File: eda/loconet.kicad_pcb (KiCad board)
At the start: 4 copper layers, 105.7 x 60.2 mm, 69 parts, among them J1 RJ12, J10 FROG4, J11 LN Debug, J12 LN Raw, J13 Input voltage, J2 DCC IN, J3 FROG1, J4 DCC1, J5 FROG2, J6 DCC2, J7 DCC3, J8 FROG3, J9 DCC4, Q2 MMBT3904, U1 LM311, U2 MOUDLE-SEEEDUINO-XIAO, U3 L78M05ABDT-TR, U4 6N139, U5 6N139, U6 6N139, U7 6N139

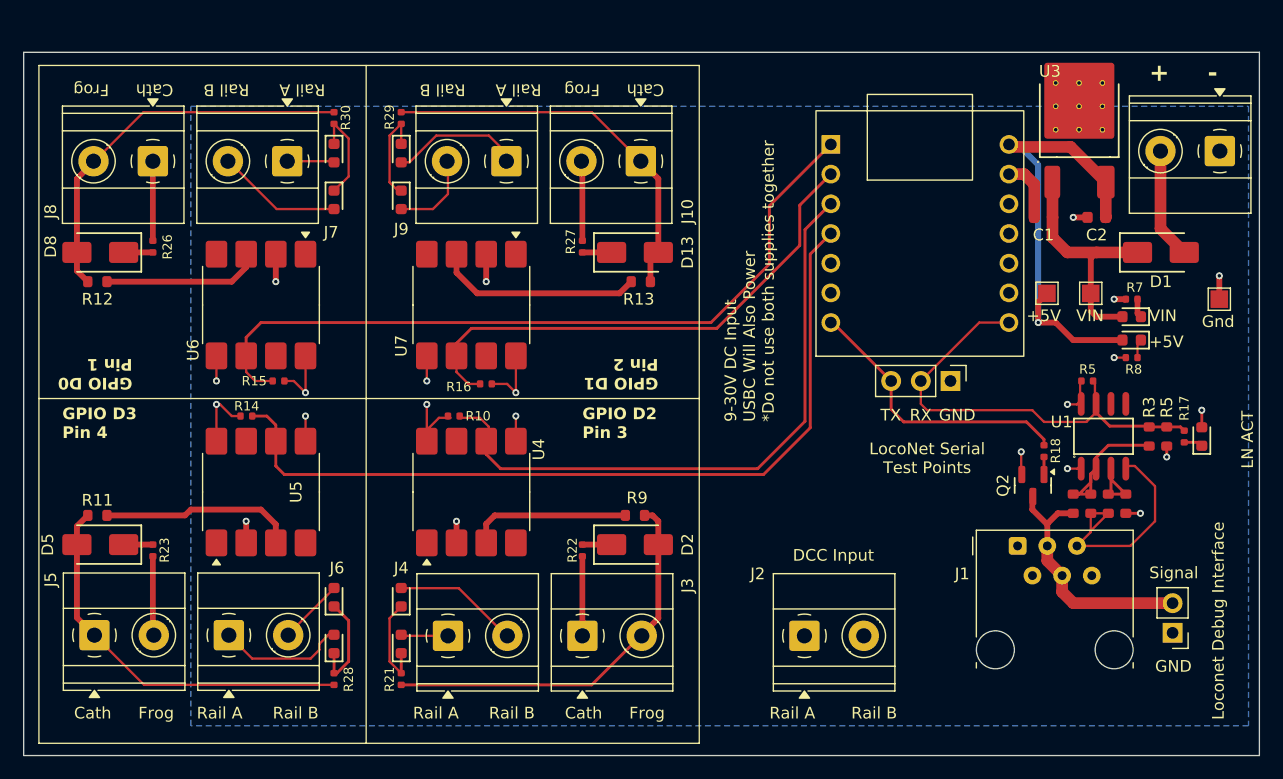
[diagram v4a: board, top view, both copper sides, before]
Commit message: Updates
* Made it possible to power with DCC. You still need a DCC input for the IO, but you can also drive this with DCC.
* Added some screen printing for help
* Added 3 GPIO headers. You can connect them how you want, but they aren't protected, so don't do anything dumb.
* updated readme
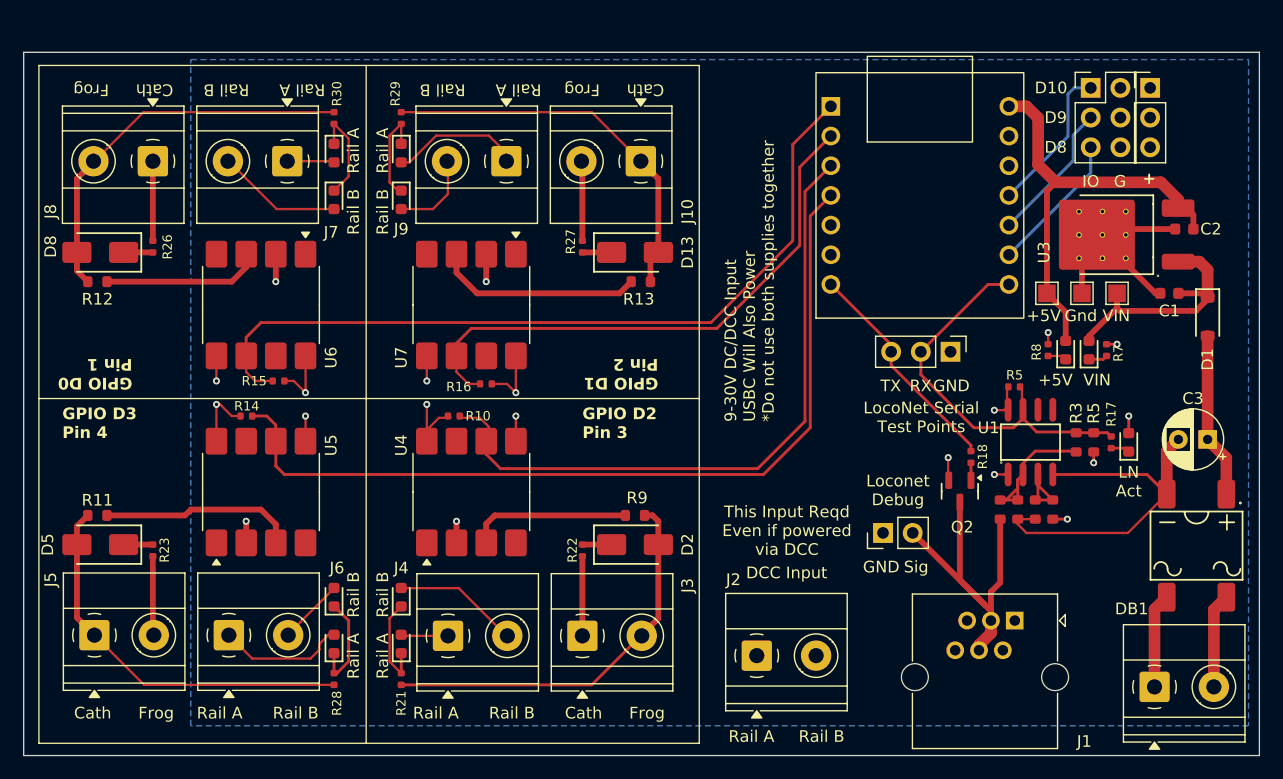
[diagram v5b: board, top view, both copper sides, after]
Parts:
- added C3: 100uf, Capacitor_THT:CP_Radial_D5.0mm_P2.50mm, F.Cu at (194.0, 105.0)
- added DB1: DB107S, PCM_JLCPCB:DBS_L8.2-W6.4-P5.10-LS10.0-BL, F.Cu at (193.1, 114.1)
- added J14: IO, Connector_PinHeader_2.54mm:PinHeader_2x03_P2.54mm_Vertical, F.Cu at (184.0, 74.9)
- added J15: Power, Connector_PinHeader_2.54mm:PinHeader_1x03_P2.54mm_Vertical, F.Cu at (189.1, 74.9)
- D1: value SS14 -> RB160M-30; footprint PCM_JLCPCB:D_SMA -> PCM_JLCPCB:D_SOD-123
- J1: footprint Connector_RJ:RJ12_Amphenol_54601-x06_Horizontal -> Connector_RJ:RJ25_Wayconn_MJEA-660X1_Horizontal
- moved J13 46.2 mm to (189.5, 126.2), turned to 0 degrees
- moved J12 26.2 mm to (166.2, 113.0), turned to 90 degrees
- moved C1 12.6 mm to (190.7, 92.5)
- moved TP3 11.8 mm to (183.2, 92.5)
- moved U3 9.43 mm to (188.0, 87.5), turned to 180 degrees
- moved C2 7.57 mm to (192.0, 87.0)
- moved R8 7.17 mm to (180.4, 97.4), turned to 90 degrees
- moved D1 6.80 mm to (194.0, 94.5), turned to -90 degrees
- moved J1 6.39 mm to (177.5, 120.5)
- moved D16 6.27 mm to (187.2, 105.2)
- moved Q2 6.27 mm to (172.8, 109.4)
- moved R1 6.27 mm to (176.2, 111.0)
- moved R17 6.27 mm to (185.8, 105.2)
- moved R18 6.27 mm to (173.8, 106.5)
- moved R2 6.27 mm to (177.8, 111.0)
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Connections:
- D1 pad 2: Net-(J13-Pin_2) -> Net-(DB1-+)
- J13 pad 1: GND -> Net-(J13-Pin_1)
- U2 pad 10: unconnected-(U2-PA5_A9_D9_MISO-Pad10) -> IO2
- U2 pad 11: unconnected-(U2-PA6_A10_D10_MOSI-Pad11) -> IO3
- U2 pad 9: unconnected-(U2-PA7_A8_D8_SCK-Pad9) -> IO1
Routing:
- net GND: track 43.4 -> 65.4 mm, vias 10 -> 8
- net Net-(DB1-+): track 0.00 -> 14.2 mm
- net IO3: track 0.00 -> 12.9 mm
- net IO2: track 0.00 -> 12.1 mm
- net IO1: track 0.00 -> 12.1 mm
- net /LNET: track 22.2 -> 31.8 mm
- net Net-(J13-Pin_1): track 0.00 -> 8.61 mm
- net TX: track 24.3 -> 19.2 mm
- net RX: track 39.9 -> 35.3 mm
- net DIP_STATE_3: track 65.3 -> 68.6 mm
- net DIP_STATE_1: track 54.1 -> 57.3 mm
- net DIP_STATE_4: track 44.9 -> 48.2 mm
- net DIP_STATE_2: track 71.8 -> 75.0 mm
- net +5V: track 40.0 -> 38.2 mm, vias 1 -> 0
- net Net-(J13-Pin_2): track 9.52 -> 8.11 mm
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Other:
- board text added: "9-30V DC/DCC Input USBC Will Also Power *Do not use both supplies together"
- board text added: "D10"
- board text added: "D8"
- board text added: "D9"
- board text added: "G"
- board text added: "IO"
- board text added: "LN Act"
- board text added: "Loconet Debug"
- board text added: "Sig"
- board text added: "This Input Reqd Even if powered via DCC"
- board text removed: "-"
- board text removed: "9-30V DC Input USBC Will Also Power *Do not use both supplies together"
- board text removed: "LN ACT"
- board text removed: "Loconet Debug Interface"
- board text removed: "Signal"

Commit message: Fixes
* Bumped the turnout indicator LED resistor to a 125mw 0805 as the 62.5mw was likely going to be too small. This allows some headroom.
* Updated README.
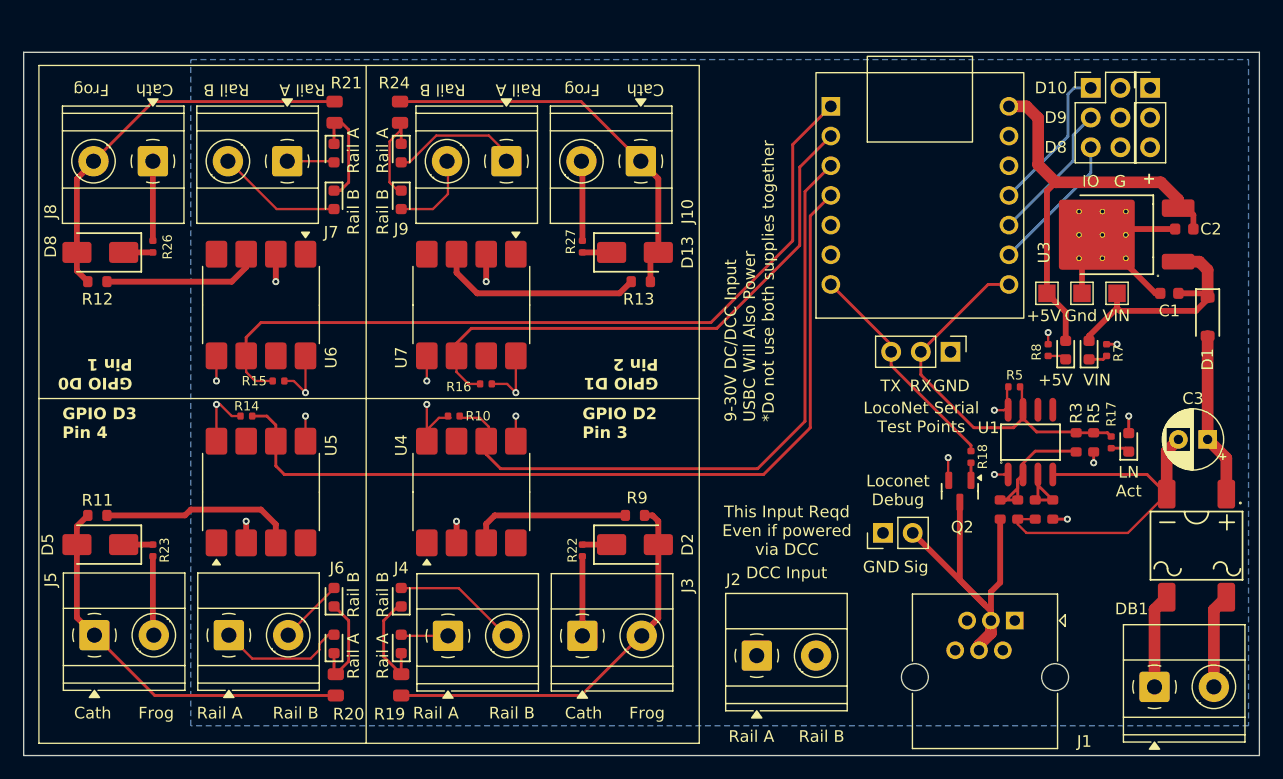
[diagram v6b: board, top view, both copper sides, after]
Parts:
- removed R28, R29, R30: 2kΩ, PCM_JLCPCB:R_0402
- added R19: 2kΩ, PCM_JLCPCB:R_0805, F.Cu at (125.0, 126.0)
- added R20: 2kΩ, PCM_JLCPCB:R_0805, F.Cu at (119.4, 126.0)
- added R24: 2kΩ, PCM_JLCPCB:R_0805, F.Cu at (124.9, 77.0)
- R21: footprint PCM_JLCPCB:R_0402 -> PCM_JLCPCB:R_0805
- moved R21 48.8 mm to (119.3, 77.0)
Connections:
- R21 pad 1: Net-(D10-Pad1) -> Net-(J8-Pin_2)
- R21 pad 2: Net-(J3-Pin_2) -> Net-(D14-Pad1)
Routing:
- net Net-(D14-Pad1): track 8.48 -> 9.31 mm
- net Net-(D10-Pad1): track 8.23 -> 9.01 mm
- net Net-(J5-Pin_1): track 33.5 -> 34.0 mm
- net Net-(J8-Pin_2): track 33.5 -> 34.1 mm

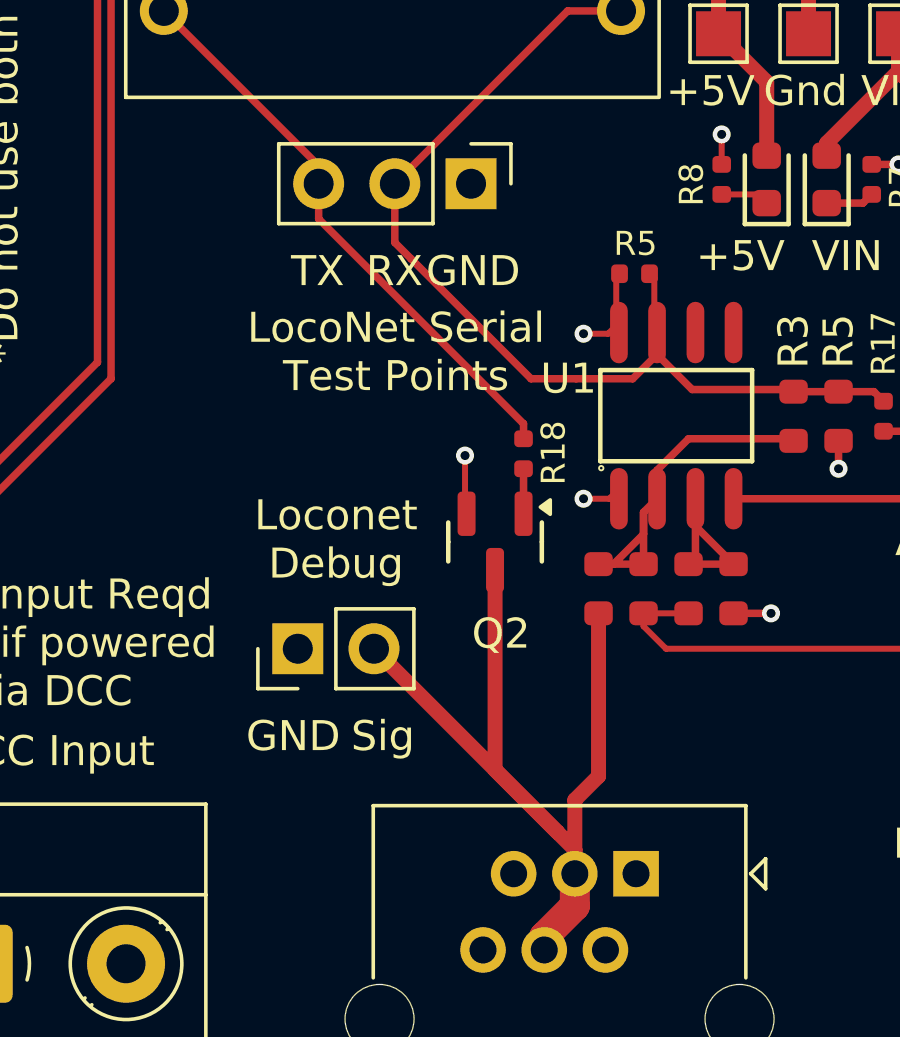
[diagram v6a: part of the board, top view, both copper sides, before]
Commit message: checkpoint, as this board is too expensive.
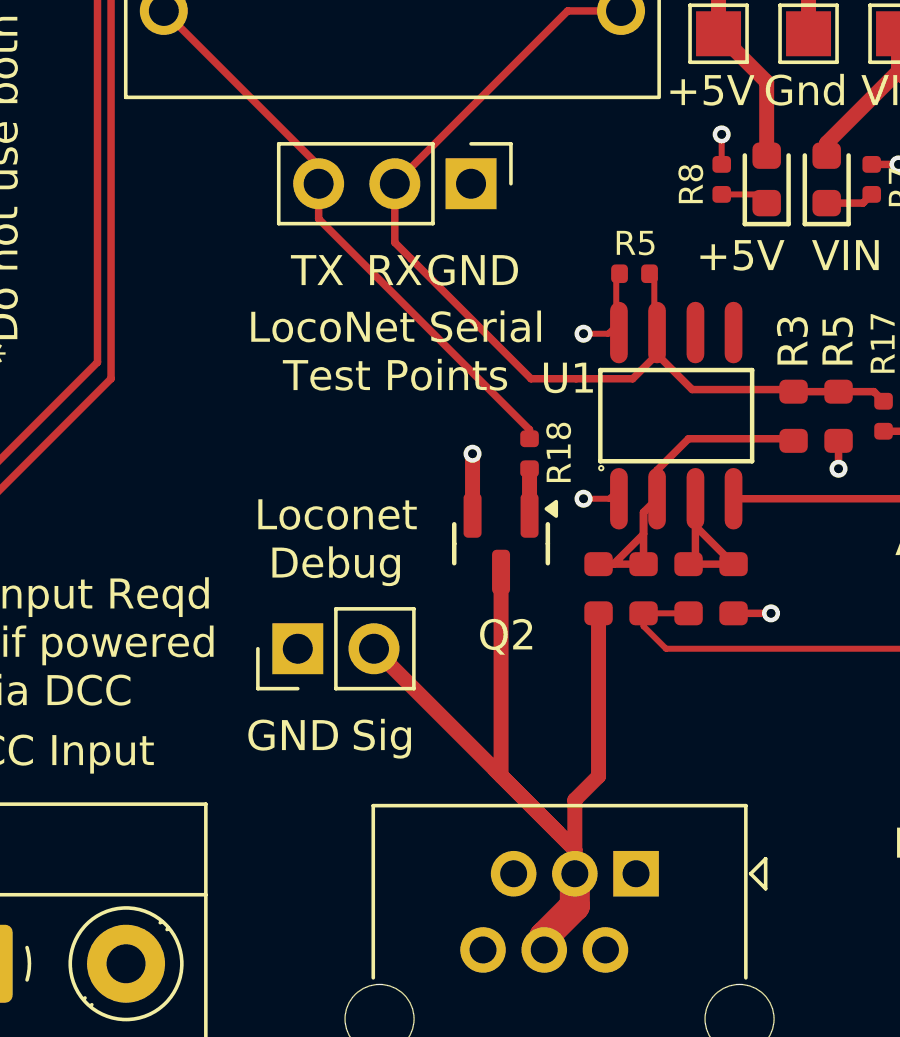
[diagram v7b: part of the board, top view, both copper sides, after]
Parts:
- moved Q2 0.21 mm to (173.0, 109.5)
- moved R18 0.20 mm to (173.9, 106.5)
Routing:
- net /LNET: track 31.8 -> 35.4 mm
- net GND: track 65.4 -> 65.9 mm
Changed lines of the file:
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@@
 	(footprint "PCM_JLCPCB:Q_SOT-23"
 		(layer "F.Cu")
-		(at 172.8 109.44 -90)
+		(at 173 109.5 -90)
 		(descr "SOT, 3 Pin (https://www.jedec.org/system/files/docs/to-236h.pdf variant AB), generated with kicad-footprint-generator ipc_gullwing_generator.py")
 		(tags "SOT TO_SOT_SMD")
 		(property "Reference" "Q2"
-			(at 3.06 -0.2 180)
+			(at 3.06 -0.2 0)
 			(layer "F.SilkS")
 			(effects
@@
 		(sheetname "/")
 		(sheetfile "loconet.kicad_sch")
-		(attr through_hole)
+		(attr through_hole exclude_from_bom dnp)
 		(fp_line
 			(start 3.851 -0.284)
@@
 	(footprint "PCM_JLCPCB:R_0402"
 		(layer "F.Cu")
-		(at 173.75 106.5 90)
+		(at 173.95 106.5 90)
 		(descr "Resistor SMD 0402 (1005 Metric), square (rectangular) end terminal, IPC_7351 nominal, (Body size source: IPC-SM-782 page 72, https://www.pcb-3d.com/wordpress/wp-content/uploads/ipc-sm-782a_amendment_1_and_2.pdf), generated with kicad-footprint-generator")
 		(tags "resistor")
@@
 	)
 	(segment
-		(start 171.8 108.06)
-		(end 171.8 106.56)
-		(width 0.2)
+		(start 172.05 106.5)
+		(end 172.05 108.56)
+		(width 0.5)
 		(layer "F.Cu")
 		(net 1)
@@
 	)
 	(via
-		(at 171.8 106.56)
+		(at 172.05 106.5)
 		(size 0.6)
 		(drill 0.3)
@@
 	)
 	(segment
-		(start 173.75 106)
-		(end 173.75 105.5)
+		(start 166.92 96.9)
+		(end 166.92 97.5)
 		(width 0.25)
 		(layer "F.Cu")
@@
 	)
 	(segment
-		(start 166.92 96.9)
-		(end 166.92 97.5)
+		(start 173.95 105.7)
+		(end 173.95 106)
 		(width 0.25)
 		(layer "F.Cu")
@@
 	)
 	(segment
-		(start 173.75 105.5)
-		(end 166.92 98.67)
+		(start 161.76 91.74)
+		(end 166.92 96.9)
 		(width 0.25)
 		(layer "F.Cu")
@@
 	(segment
 		(start 166.92 98.67)
-		(end 166.92 97.5)
+		(end 173.95 105.7)
 		(width 0.25)
 		(layer "F.Cu")
@@
 	)
 	(segment
-		(start 161.76 91.74)
-		(end 166.92 96.9)
+		(start 166.92 97.5)
+		(end 166.92 98.67)
 		(width 0.25)
 		(layer "F.Cu")
@@
 	)
 	(segment
-		(start 174.8825 119.1175)
+		(start 175.3825 119.6175)
 		(end 175.46 119.695)
 		(width 0.5)
@@
 	)
 	(segment
+		(start 174.8825 119.1175)
+		(end 175.3825 119.6175)
+		(width 0.5)
+		(layer "F.Cu")
+		(net 41)
+	)
+	(segment
 		(start 172.8 117.035)
 		(end 174.8825 119.1175)
@@
 	)
 	(segment
-		(start 172.8 110.38)
-		(end 172.8 117.035)
+		(start 173 110.44)
+		(end 173 117.235)
 		(width 0.5)
 		(layer "F.Cu")
@@
 	)
 	(segment
+		(start 173 117.235)
+		(end 175.3825 119.6175)
+		(width 0.5)
+		(layer "F.Cu")
+		(net 41)
+	)
+	(segment
 		(start 132.27 112.23)
 		(end 132.27 113.85)
@@
 	)
 	(segment
-		(start 173.75 108.5)
-		(end 173.75 107)
-		(width 0.25)
+		(start 173.95 107)
+		(end 173.95 108.56)
+		(width 0.5)
 		(layer "F.Cu")
 		(net 51)

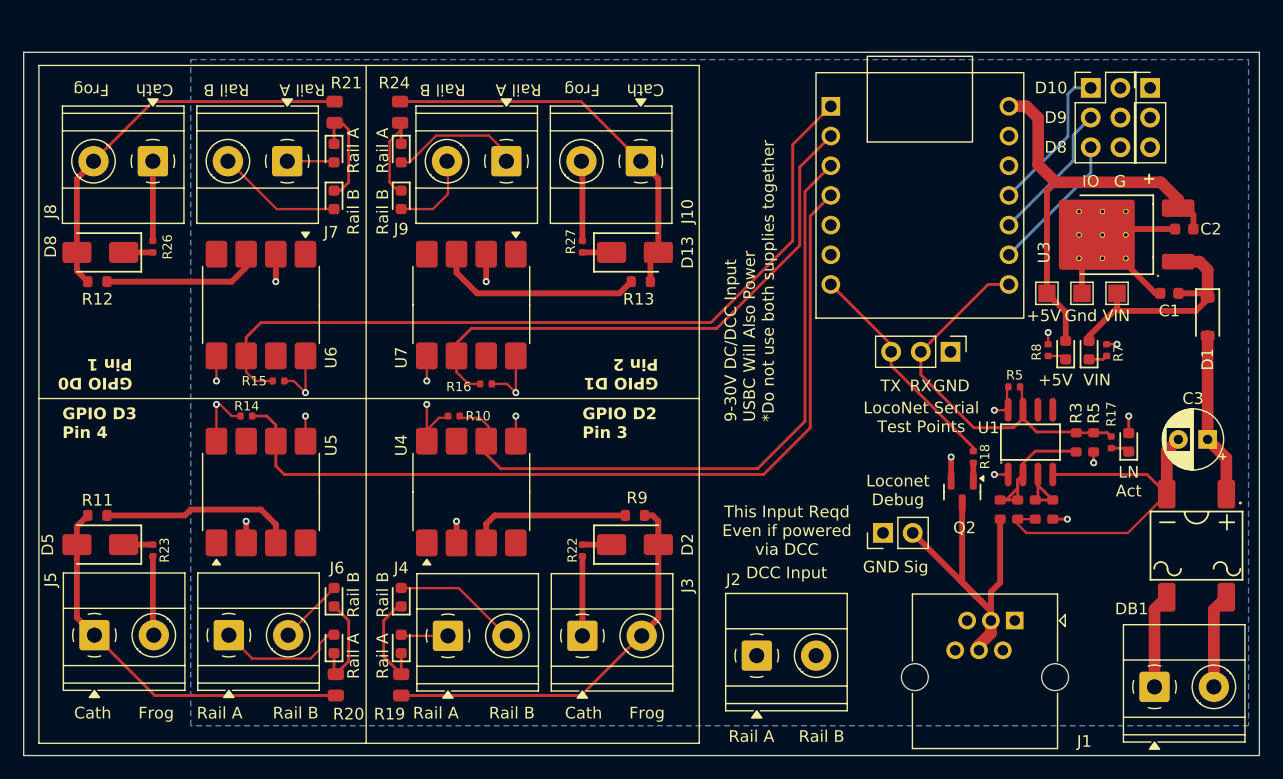
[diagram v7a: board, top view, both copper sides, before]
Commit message: Fixes for cost reasons
* Moved to a 2 layer board to try to make this cheaper
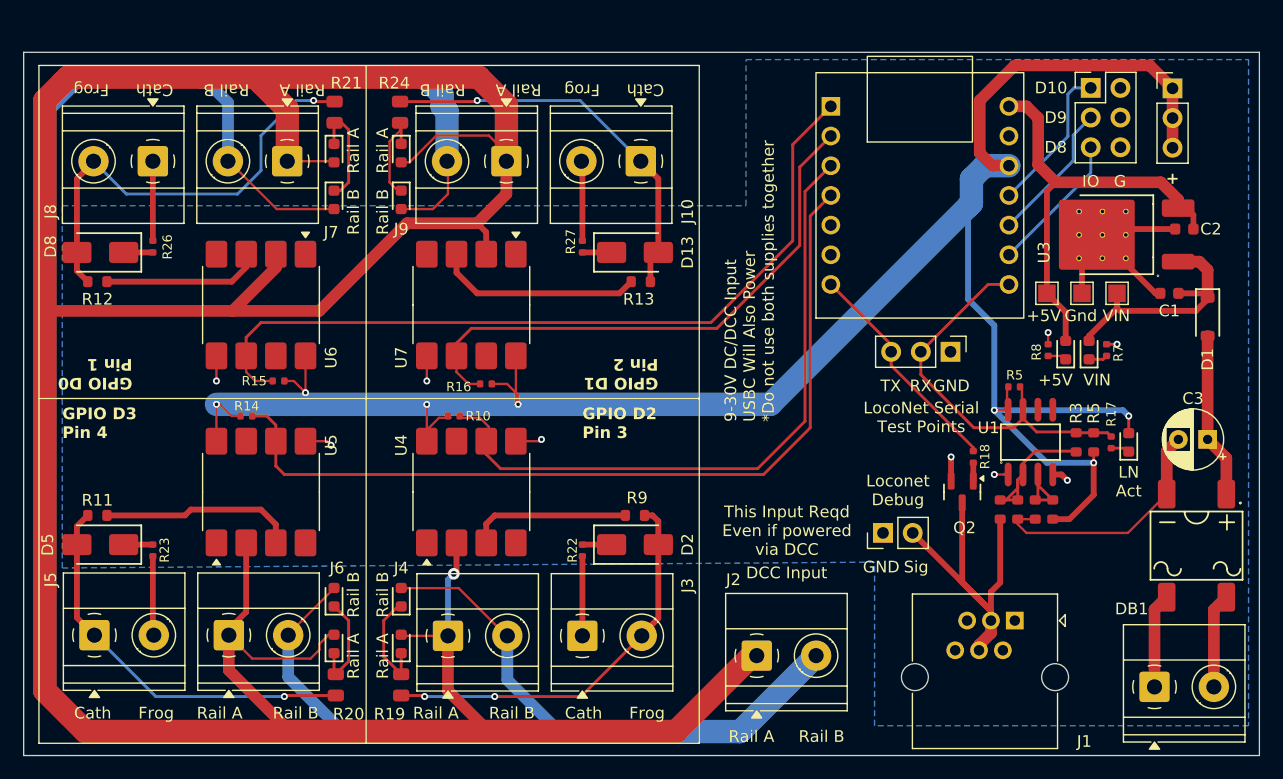
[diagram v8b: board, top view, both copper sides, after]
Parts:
- moved J15 1.92 mm to (191.0, 75.0)
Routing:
- net DCC_A: track 39.4 -> 293.9 mm, vias 4 -> 1
- net DCC_B: track 34.5 -> 224.9 mm
- net +3V3: track 30.1 -> 187.5 mm, vias 8 -> 7
- net GND: track 65.9 -> 57.2 mm, vias 8 -> 9
- net Net-(J8-Pin_2): track 34.1 -> 38.2 mm, vias 0 -> 1
- net Net-(J3-Pin_2): track 34.4 -> 34.6 mm, vias 0 -> 2
- net Net-(J10-Pin_1): track 33.9 -> 34.0 mm, vias 0 -> 1
- net Net-(J5-Pin_1): track 34.0 -> 34.1 mm, vias 0 -> 1
- removed copper zone on In1.Cu, net +3V3
- removed copper zone on In1.Cu, net DCC_A
- removed copper zone on In2.Cu, net DCC_B
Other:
- copper layers 4 -> 2
